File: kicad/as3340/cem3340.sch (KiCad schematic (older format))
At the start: 54 parts, among them U10 LM79L05, U11 LM393, U2 TL074, U3 AS3340, U4 DG303B, U9 DG442CY+

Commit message: start revision 0.3 of board
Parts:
- removed D1, D2: 1N5819, Diode_SMD:D_SOD-323, symbol Diode:1N5819
- removed R26: 5k6, Resistor_SMD:R_0603_1608Metric, symbol Device:R
- removed R39: 100k 0.1%, Resistor_SMD:R_0603_1608Metric, symbol Device:R
- removed TP3: TestPoint, TestPoint:TestPoint_Pad_2.0x2.0mm, symbol Connector:TestPoint
- added C33: 1n, Capacitor_SMD:C_0603_1608Metric, symbol Device:C
- added C35: 0.1u, Capacitor_SMD:C_0603_1608Metric, symbol Device:C
- added D5, D6: 1N4148W, Diode_SMD:D_SOD-123, symbol Diode:1N4148W
- added R57: 10k, Resistor_SMD:R_0603_1608Metric, symbol Device:R
- added R58: ?, Resistor_SMD:R_0603_1608Metric, symbol Device:R
- added unit 2 of U9
- C17: value 1u -> 1n; LCSC C15849 -> (none); LCSC Part C15849 -> (none)
- C21: footprint Capacitor_THT:CP_Radial_D5.0mm_P2.50mm -> Capacitor_THT:Nichicon QYX2A102KTP; Digikey QYX2A102KTP1FD -> QYX2A102KTP
- R18: value 100k -> 82k; LCSC Part C25803 -> (none)
- U10: footprint Package_TO_SOT_THT:TO-92_Inline -> Package_TO_SOT_THT:TO-92_Inline_Wide
- U4: symbol as3340-rescue:DG303B-Analog_Switch -> Analog_Switch:DG303B
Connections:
- net labels added: SYNC_NEG_CTRL, SYNC_POS_CTRL
- net labels removed: EXT_FREQ_CV, HARD_SYNC_CTRL
- wire segments 190 -> 197
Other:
- note added: "No switch on LINEAR_FM_DAC:\nEither drive it or disable (High-Z) via cmd to DAC"
- note added: "PWM control is 0 - 5V per datasheet at +15 V supply. Specifically, it’s zero to Sawtooth level / 2, so 0 - 4V w/ +12"
- note added: "TODO: A lot todo here.\nCheck hard sync voltage level; adjust pullup/down R"
- note removed: "NO - PWM in is 0 - 5V positive"
- note removed: "No switch on LINEAR_FM_DAC:\nDisable (High-Z) via cmd to DAC"
- note removed: "TODO: Check hard sync voltage level; adjust pullup/down R"
- moved on the sheet: C17, R28, R42, U2B

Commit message: routed v0.3
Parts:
- removed unit 2 of U2
- removed U4: DG303B, Package_SO:SOIC-14_3.9x8.7mm_P1.27mm, symbol Analog_Switch:DG303B
- added TP1: TestPoint, TestPoint:TestPoint_Pad_2.0x2.0mm, symbol Connector:TestPoint
- added U8: DG442CY+, Package_SO:SOIC-16_3.9x9.9mm_P1.27mm, symbol Analog_Switch:DG441xY
- C17, C33: value 1n -> 10n
- R58: value ? -> 220k
- renumbered D6 to D1, D5 to D2
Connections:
- net +12V: now also R57.2; no longer R28.2
- net -12V: no longer R57.1
- net -5V: now also R28.1
- net EXT_MOD_PW_CTRL: now also U8.9
- net HARD_SYNC: now also D1.2 (A), D2.1 (K), TP1.1; no longer D1.1 (K), D2.2 (A)
- net SCALED_MOD_BUFFERED: now also U2.1, U2.2 (-), U8.10
- net SYNC_NEG_CTRL: now also U9.8; no longer U9.9
- net SYNC_POS_CTRL: now also U9.9; no longer U9.8
- net at R18.2: now also U8.11
- new net: C17.1, D2.2 (A), R28.2
- new net: C33.1, D1.1 (K), R57.1
- no-connect marks 2 -> 0
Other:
- note added: "TODO: AC Couple external signal"
- note added: "TODO: check modulation signal R value"
- note removed: "TODO: A lot todo here.\nCheck hard sync voltage level; adjust pullup/down R"
- note removed: "TODO: R values will need to be adjusted"
- moved on the sheet: C17, C23, C33, D1, D2, R28, R37, R42, R46, R57, RV2, U2A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

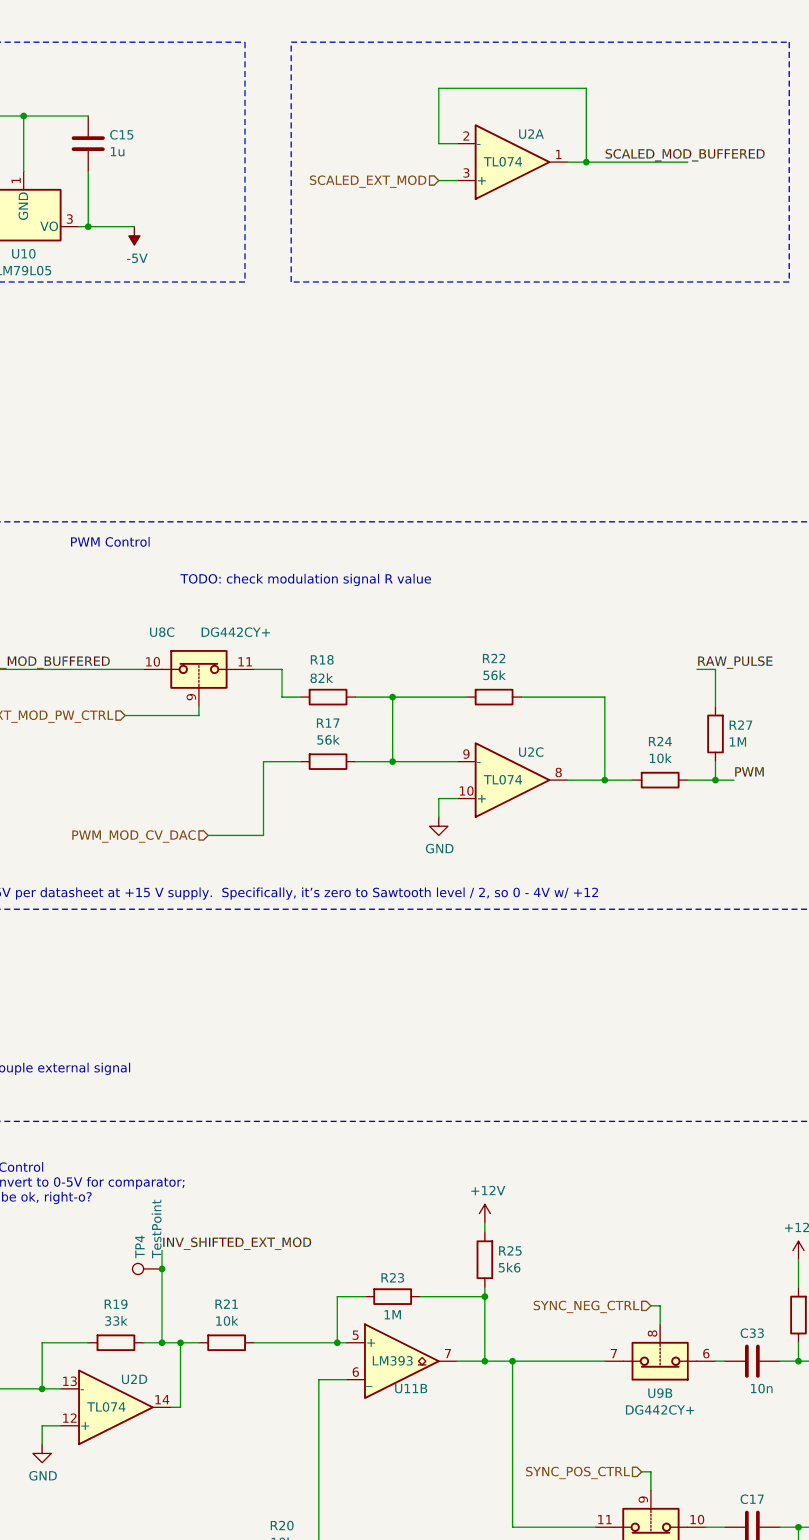
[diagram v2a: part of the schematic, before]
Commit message: rework output stage
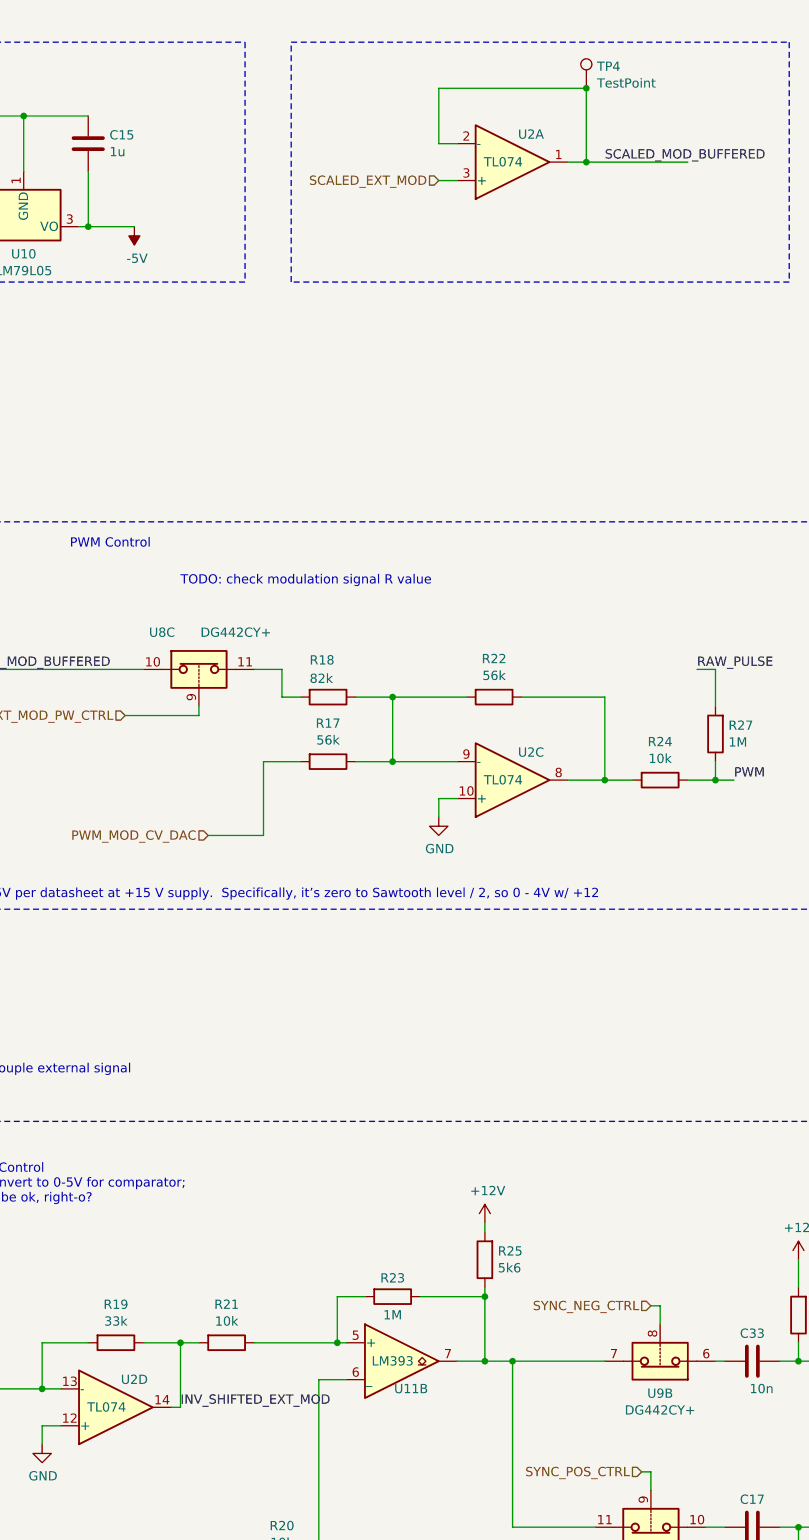
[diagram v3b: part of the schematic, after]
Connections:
- net INV_SHIFTED_EXT_MOD: no longer TP4.1
- net SCALED_MOD_BUFFERED: now also TP4.1
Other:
- moved on the sheet: TP4
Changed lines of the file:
@@
 	2100 8100 2200 8100
 Wire Wire Line
-	2650 7850 2750 7850
-Wire Wire Line
 	2850 8200 2800 8200
-Text Label 2750 7350 0    50   ~ 0
+Text Label 2850 8200 0    50   ~ 0
 INV_SHIFTED_EXT_MOD
 Wire Wire Line
@@
 Wire Wire Line
 	4350 7950 4500 7950
-Connection ~ 2750 7850
-Wire Wire Line
-	2750 7850 2850 7850
 Wire Wire Line
 	3850 7600 3700 7600
@@
 Wire Notes Line
 	750  9800 750  6650
-Wire Wire Line
-	2750 7350 2750 7450
 Wire Wire Line
 	14300 6800 14300 6500
@@
 L Connector:TestPoint TP4
 U 1 1 631E8ACB
-P 2750 7450
-F 0 "TP4" H 2808 7568 50  0000 L CNN
-F 1 "TestPoint" H 2808 7477 50  0000 L CNN
-F 2 "TestPoint:TestPoint_Pad_2.0x2.0mm" H 2950 7450 50  0001 C CNN
-F 3 "~" H 2950 7450 50  0001 C CNN
-F 4 "952-2664-6-ND" H 2750 7450 50  0001 C CNN "Digikey"
-	1    2750 7450
-	0    -1   -1   0
-$EndComp
-Connection ~ 2750 7450
-Wire Wire Line
-	2750 7450 2750 7850
+P 5050 1050
+F 0 "TP4" H 5108 1168 50  0000 L CNN
+F 1 "TestPoint" H 5108 1077 50  0000 L CNN
+F 2 "TestPoint:TestPoint_Pad_2.0x2.0mm" H 5250 1050 50  0001 C CNN
+F 3 "~" H 5250 1050 50  0001 C CNN
+F 4 "952-2664-6-ND" H 5050 1050 50  0001 C CNN "Digikey"
+	1    5050 1050
+	1    0    0    -1
+$EndComp
 $Comp
 L Device:C C33
@@
 Wire Wire Line
 	6200 8850 6350 8850
+Wire Wire Line
+	2650 7850 2850 7850
+Connection ~ 5050 1050
 $EndSCHEMATC

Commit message: testing...
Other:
- note added: "TODO: check modulation signal R value\nTODO: should scaled_mod be re-inverted?"
- note removed: "TODO: check modulation signal R value"
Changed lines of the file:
@@
 Wire Wire Line
 	2550 4450 2950 4450
-Text Notes 2850 3750 0    50   ~ 0
-TODO: check modulation signal R value
+Text Notes 2850 3750 0    50   Italic 10
+TODO: check modulation signal R value\nTODO: should scaled_mod be re-inverted?
 Text Notes 1450 6400 0    50   ~ 0
 TODO: AC Couple external signal

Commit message: routed for v0.3 -- perhaps final
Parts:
- added TP5: TestPoint, TestPoint:TestPoint_Pad_2.0x2.0mm, symbol Connector:TestPoint
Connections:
- net -5V: now also R36.2
- net EXP_FM_EXT_CTRL: now also U9.1; no longer U9.16
- net GND: no longer R36.2
- net INV_SHIFTED_EXT_MOD: now also TP5.1
- net LINEAR_FM: now also U9.15; no longer R30.1
- net LINEAR_FM_EXT_CTRL: now also U9.16; no longer U9.1
- net SCALED_MOD_BUFFERED: now also C18.2, R18.2, R42.2; no longer U8.10, U9.14, U9.3
- net SUMMING_INPUT: now also U9.2; no longer R42.1
- net at R17.1, R22.2, U2.9 (-): now also U8.11; no longer R18.1
- new net: R18.1, U8.10
- new net: R42.1, U9.3
- new net: R30.1, U9.14
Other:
- note added: "3340; Pulse pulldown per AS spec (51k); not CEM (10k)\nPulse: -5 : approx 10.5V\nSaw: 0 : 8V\nTri: 0 : 4V\nComparator: -5 : 5V"
- note added: "Hard Sync Selection and Control\nOSC_EXTERNAL: assume somewhere around +/- 5V but it could well be outside that;\nattenuate/invert external to 0-5V for both 393 comparators;\nkeep external signal inside -5 : +12"
- note added: "PWM Control: external signal biased by DAC since it’s an inversion mess"
- note removed: "3340; Pulse pulldown per AS spec (51k); not CEM (10k)\nPulse: 0 : approx 10.5V\nSaw: 0 : 8V\nTri: 0 : 4V\nComparator: 0 : 5V"
- note removed: "Hard Sync Selection and Control\nOSC_EXTERNAL: +/- 5V; invert to 0-5V for comparator;\nphase inversion ought to be ok, right-o?"
- note removed: "PWM Control"
- note removed: "TODO: AC Couple external signal"
- note removed: "TODO: check modulation signal R value\nTODO: should scaled_mod be re-inverted?"
- moved on the sheet: C18, R18, R20, R21, R30, R42, U8C

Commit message: update gerber files and assembly
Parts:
- C17, C33: LCSC Part (none) -> C57112
- R17, R22: LCSC Part C23184 -> C23206
- R18: LCSC Part (none) -> C23254
- R36: value 51K -> 51k
- R58: LCSC Part (none) -> C22961
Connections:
- net -5V: no longer R36.2
- net GND: now also R36.2
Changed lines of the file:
@@
 F 2 "Capacitor_SMD:C_0603_1608Metric" H 5988 8700 50  0001 C CNN
 F 3 "~" H 5950 8850 50  0001 C CNN
-F 4 "" H 5950 8850 50  0001 C CNN "LCSC Part"
+F 4 "C57112" H 5950 8850 50  0001 C CNN "LCSC Part"
 	1    5950 8850
 	0    1    1    0
@@
 F 2 "Resistor_SMD:R_0603_1608Metric" V 3580 4700 50  0001 C CNN
 F 3 "~" H 3650 4700 50  0001 C CNN
-F 4 "C23184" H 3650 4700 50  0001 C CNN "LCSC Part"
+F 4 "C23206" H 3650 4700 50  0001 C CNN "LCSC Part"
 	1    3650 4700
 	0    1    1    0
@@
 F 2 "Resistor_SMD:R_0603_1608Metric" V 4480 4350 50  0001 C CNN
 F 3 "~" H 4550 4350 50  0001 C CNN
-F 4 "C23184" H 4550 4350 50  0001 C CNN "LCSC Part"
+F 4 "C23206" H 4550 4350 50  0001 C CNN "LCSC Part"
 	1    4550 4350
 	0    1    1    0
@@
 P 12550 6200
 F 0 "R36" H 12620 6246 50  0000 L CNN
-F 1 "51K" H 12620 6155 50  0000 L CNN
+F 1 "51k" H 12620 6155 50  0000 L CNN
 F 2 "Resistor_SMD:R_0603_1608Metric" V 12480 6200 50  0001 C CNN
 F 3 "~" H 12550 6200 50  0001 C CNN
@@
 F 2 "Capacitor_SMD:C_0603_1608Metric" H 5988 7800 50  0001 C CNN
 F 3 "~" H 5950 7950 50  0001 C CNN
-F 4 "" H 5950 7950 50  0001 C CNN "LCSC Part"
+F 4 "C57112" H 5950 7950 50  0001 C CNN "LCSC Part"
 	1    5950 7950
 	0    1    1    0
@@
 F 2 "Resistor_SMD:R_0603_1608Metric" V 14680 1750 50  0001 C CNN
 F 3 "" H 14750 1750 50  0001 C CNN
-F 4 "" H 14750 1750 50  0001 C CNN "LCSC Part"
+F 4 "C22961" H 14750 1750 50  0001 C CNN "LCSC Part"
 	1    14750 1750
 	1    0    0    -1
@@
 F 2 "Resistor_SMD:R_0603_1608Metric" V 2430 4350 50  0001 C CNN
 F 3 "~" H 2500 4350 50  0001 C CNN
-F 4 "" H 2500 4350 50  0001 C CNN "LCSC Part"
+F 4 "C23254" H 2500 4350 50  0001 C CNN "LCSC Part"
 	1    2500 4350
 	0    1    1    0
@@
 Text Label 12100 2400 0    50   ~ 0
 SCALED_MOD_BUFFERED
-$Comp
-L power:-5V #PWR015
-U 1 1 637034E0
-P 12550 6350
-F 0 "#PWR015" H 12550 6450 50  0001 C CNN
-F 1 "-5V" H 12565 6523 50  0000 C CNN
-F 2 "" H 12550 6350 50  0001 C CNN
-F 3 "" H 12550 6350 50  0001 C CNN
-	1    12550 6350
-	1    0    0    1
-$EndComp
 $Comp
 L Analog_Switch:DG441xY U9
@@
 Wire Wire Line
 	13000 2400 12100 2400
+$Comp
+L power:GND #PWR015
+U 1 1 62AE1982
+P 12550 6400
+F 0 "#PWR015" H 12550 6150 50  0001 C CNN
+F 1 "GND" H 12555 6227 50  0000 C CNN
+F 2 "" H 12550 6400 50  0001 C CNN
+F 3 "" H 12550 6400 50  0001 C CNN
+	1    12550 6400
+	1    0    0    -1
+$EndComp
+Wire Wire Line
+	12550 6400 12550 6350
 $EndSCHEMATC

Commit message: v0.3 submitted to jlcpcb
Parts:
- removed R20, R40: 10k, Resistor_SMD:R_0603_1608Metric, symbol Device:R
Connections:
- net SYNC_LEVEL_CV_DAC: now also U11.6 (_)
- net VCO_SAW: now also U11.2 (-)
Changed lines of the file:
@@
 	0    1    1    0
 $EndComp
-Text HLabel 3000 9000 0    50   Input ~ 0
+Text HLabel 3300 9000 0    50   Input ~ 0
 SYNC_LEVEL_CV_DAC
 Text Label 6950 8350 0    50   ~ 0
@@
 F 4 "C22935" H 4000 7600 50  0001 C CNN "LCSC Part"
 	1    4000 7600
-	0    1    1    0
-$EndComp
-$Comp
-L Device:R R20
-U 1 1 6211CB96
-P 3400 9000
-F 0 "R20" V 3193 9000 50  0000 C CNN
-F 1 "10k" V 3284 9000 50  0000 C CNN
-F 2 "Resistor_SMD:R_0603_1608Metric" V 3330 9000 50  0001 C CNN
-F 3 "~" H 3400 9000 50  0001 C CNN
-F 4 "C25804" H 3400 9000 50  0001 C CNN "LCSC Part"
-	1    3400 9000
 	0    1    1    0
 $EndComp
@@
 	12550 6800 13350 6800
 $Comp
-L Device:R R40
-U 1 1 64112345
-P 13350 7000
-F 0 "R40" V 13250 6900 50  0000 C CNN
-F 1 "10k" V 13450 7000 50  0000 C CNN
-F 2 "Resistor_SMD:R_0603_1608Metric" V 13280 7000 50  0001 C CNN
-F 3 "~" H 13350 7000 50  0001 C CNN
-F 4 "C25804" H 13350 7000 50  0001 C CNN "LCSC Part"
-	1    13350 7000
-	0    1    1    0
-$EndComp
-Wire Wire Line
-	13500 7000 14500 7000
-$Comp
 L Device:R R43
 U 1 1 64112351
@@
 Connection ~ 12650 7000
 Wire Wire Line
-	12650 7000 13200 7000
-Wire Wire Line
 	3600 8050 3600 9000
-Wire Wire Line
-	3600 9000 3550 9000
-Wire Wire Line
-	3250 9000 3000 9000
 Wire Wire Line
 	4350 7950 4500 7950
@@
 Wire Wire Line
 	12550 6400 12550 6350
+Wire Wire Line
+	3300 9000 3600 9000
+Wire Wire Line
+	12650 7000 14500 7000
 $EndSCHEMATC
